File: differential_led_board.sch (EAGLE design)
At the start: 51 parts, among them IC1 LD1117S33, IC2 TJA1057, IC3 AT25SF041, IC4 LMS33460, IC5 SN75175SOP-16, IC6 STM32F042F, J1 1792863, Q1 8MHz

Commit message: Finished output stage of differential LED board; started routing CANnabus controller/power sections
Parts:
- added R11, R12: 1k, rcl:R-EU_M0805
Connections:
- removed net ADC_VCC: IC6.PA0
- new net ADC_VIN: IC6.PA0, R11.1, R12.2
- net +5V: now also R11.2
- net GND: now also R12.1
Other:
- note added: "VIn Measurement"
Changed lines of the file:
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@@
 <attribute name="MOUSER" value="71-CRCW0805330RFKEAC"/>
 </part>
+<part name="R11" library="rcl" library_urn="urn:adsk.eagle:library:334" deviceset="R-EU_" device="M0805" package3d_urn="urn:adsk.eagle:package:23556/1" value="1k">
+<attribute name="MOUSER" value="755-ESR10EZPJ102"/>
+</part>
+<part name="R12" library="rcl" library_urn="urn:adsk.eagle:library:334" deviceset="R-EU_" device="M0805" package3d_urn="urn:adsk.eagle:package:23556/1" value="1k">
+<attribute name="MOUSER" value="755-ESR10EZPJ102"/>
+</part>
+<part name="GND19" library="supply1" library_urn="urn:adsk.eagle:library:371" deviceset="GND" device=""/>
+<part name="P+14" library="supply1" library_urn="urn:adsk.eagle:library:371" deviceset="+5V" device=""/>
 </parts>
 <sheets>
@@
 <text x="149.86" y="38.1" size="2.54" layer="97">CAN Transceiver</text>
 <text x="101.6" y="149.86" size="2.54" layer="97">Boot Flash</text>
+<wire x1="147.32" y1="83.82" x2="147.32" y2="147.32" width="0.1524" layer="94" style="longdash"/>
+<text x="101.6" y="86.36" size="2.54" layer="97">VIn Measurement</text>
 </plain>
 <instances>
@@
 <instance part="GND11" gate="1" x="55.88" y="7.62" smashed="yes">
 <attribute name="VALUE" x="53.34" y="5.08" size="1.778" layer="96"/>
+</instance>
+<instance part="R11" gate="G$1" x="106.68" y="134.62" smashed="yes" rot="R90">
+<attribute name="MOUSER" x="106.68" y="134.62" size="1.27" layer="96" rot="R90" align="top-center" display="off"/>
+<attribute name="NAME" x="105.1814" y="130.81" size="1.778" layer="95" rot="R90"/>
+<attribute name="VALUE" x="109.982" y="133.35" size="1.778" layer="96" rot="R90"/>
+</instance>
+<instance part="R12" gate="G$1" x="106.68" y="124.46" smashed="yes" rot="R90">
+<attribute name="MOUSER" x="106.68" y="124.46" size="1.27" layer="96" rot="R90" align="top-center" display="off"/>
+<attribute name="NAME" x="105.1814" y="120.65" size="1.778" layer="95" rot="R90"/>
+<attribute name="VALUE" x="109.982" y="123.19" size="1.778" layer="96" rot="R90"/>
+</instance>
+<instance part="GND19" gate="1" x="106.68" y="116.84" smashed="yes">
+<attribute name="VALUE" x="104.14" y="114.3" size="1.778" layer="96"/>
+</instance>
+<instance part="P+14" gate="1" x="106.68" y="142.24" smashed="yes">
+<attribute name="VALUE" x="104.14" y="137.16" size="1.778" layer="96" rot="R90"/>
 </instance>
 </instances>
@@
 <junction x="198.12" y="53.34"/>
 </segment>
+<segment>
+<pinref part="R12" gate="G$1" pin="1"/>
+<pinref part="GND19" gate="1" pin="GND"/>
+<junction x="106.68" y="119.38"/>
+</segment>
 </net>
 <net name="CAN_TX" class="0">
@@
 </segment>
 </net>
-<net name="ADC_VCC" class="0">
+<net name="ADC_VIN" class="0">
 <segment>
 <pinref part="IC6" gate="G$1" pin="PA0"/>
@@
 <junction x="68.58" y="149.86"/>
 </segment>
+<segment>
+<pinref part="R11" gate="G$1" pin="1"/>
+<pinref part="R12" gate="G$1" pin="2"/>
+<wire x1="106.68" y1="129.54" x2="111.76" y2="129.54" width="0.1524" layer="91" style="longdash"/>
+<junction x="106.68" y="129.54"/>
+<label x="111.76" y="129.54" size="1.27" layer="95" xref="yes"/>
+</segment>
 </net>
 <net name="ADC_CURRENT" class="0">
@@
 <junction x="66.04" y="17.78"/>
 </segment>
-</net>
+<segment>
+<pinref part="R11" gate="G$1" pin="2"/>
+<pinref part="P+14" gate="1" pin="+5V"/>
+<junction x="106.68" y="139.7"/>
+</segment>
+</net>

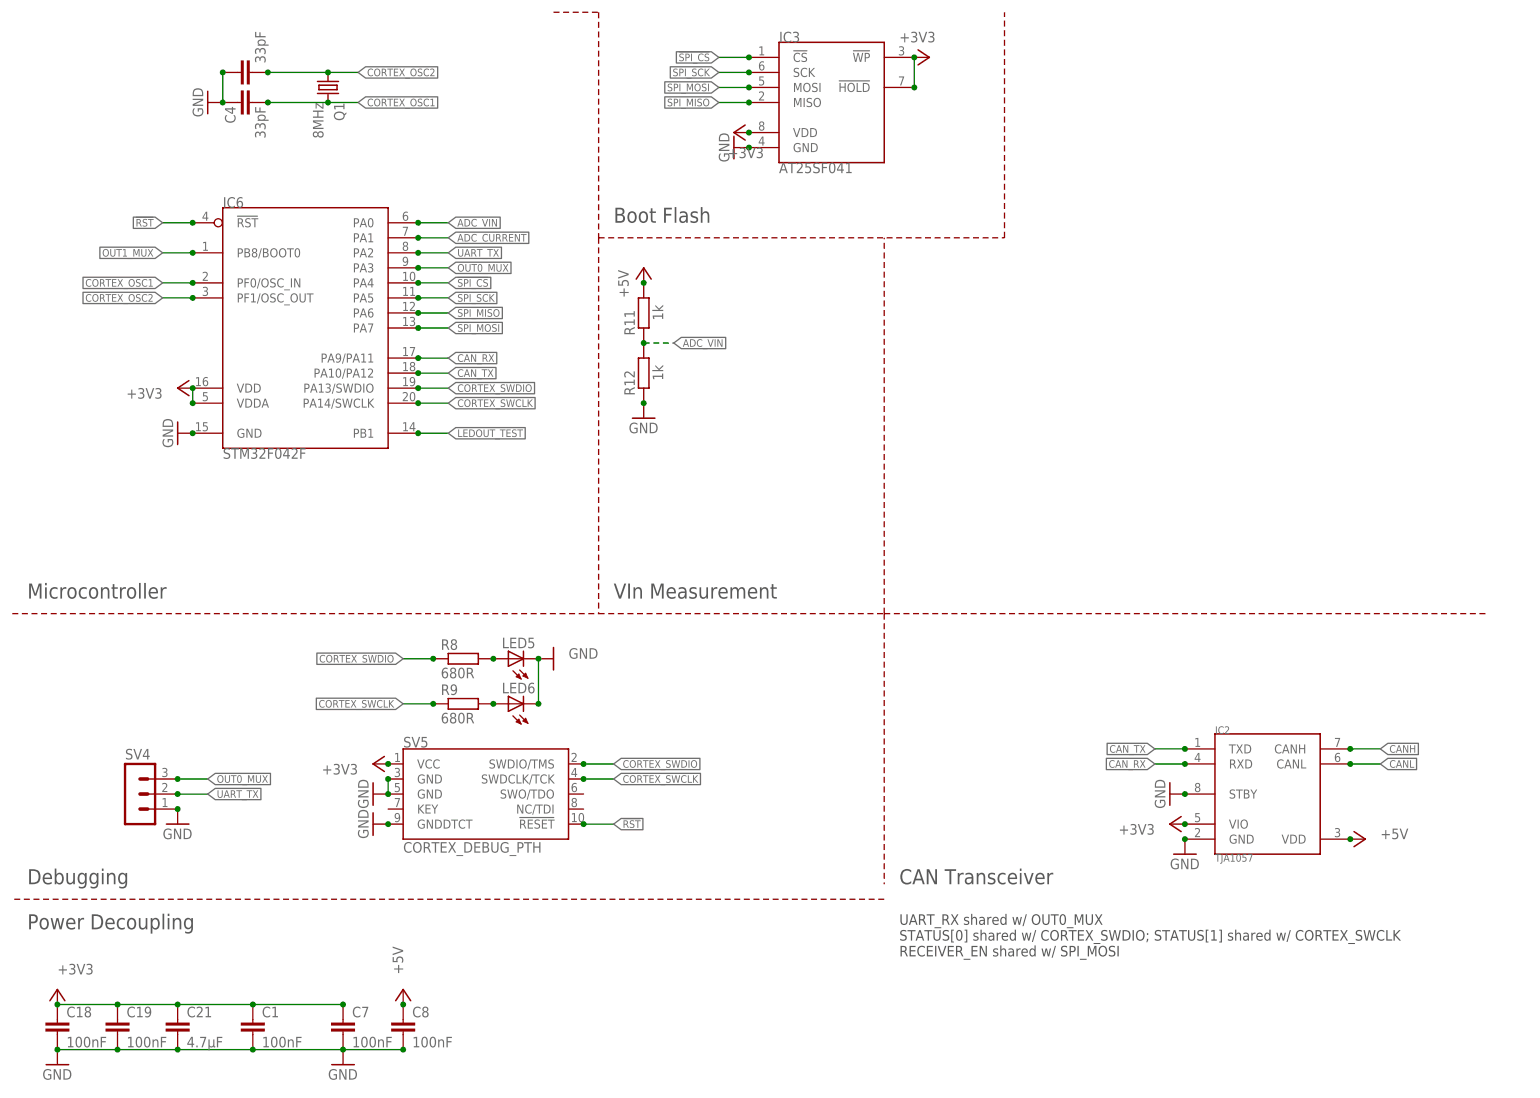
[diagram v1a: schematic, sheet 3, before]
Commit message: Added LT6100 to measure current (todo: add shunt connections)
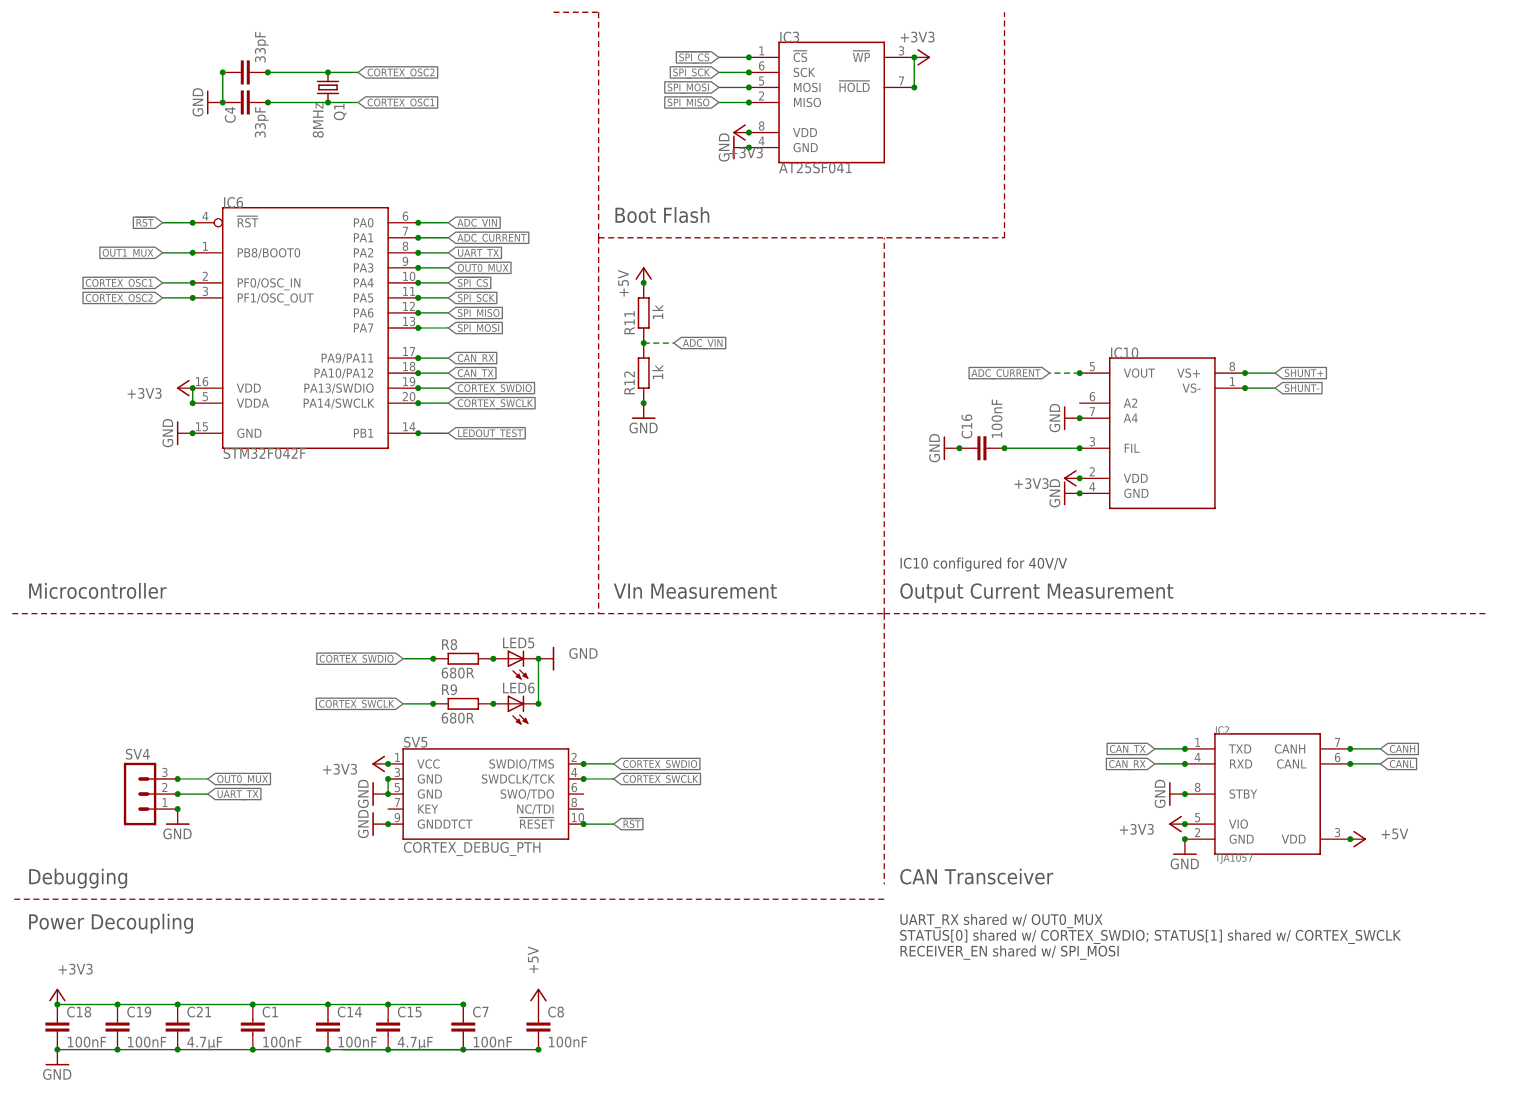
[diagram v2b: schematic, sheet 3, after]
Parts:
- added C14, C16: 100nF, rcl:C-EUC0805
- added C15: 4.7µF, rcl:C-EUC0805
- added IC10: (no value), lichtenstein_onion:LT6100MSOP-8
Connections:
- new net N$7: C16.2, IC10.FIL
- new net SHUNT+: IC10.VS+
- new net SHUNT-: IC10.VS-
- net +3V3: now also C14.1, C15.1, IC10.VDD
- net ADC_CURRENT: now also IC10.VOUT
- net GND: now also C14.2, C15.2, C16.1, IC10.A4, IC10.GND
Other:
- note added: "IC10 configured for 40V/V"
- note added: "Output Current Measurement"
- moved on the sheet: C7, C8

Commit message: finished routing LED board; substituted a few components and fixed missing level translation
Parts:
- removed C21: 4.7µF, rcl:C-EUC0805
- removed LED5: (no value), led:LEDCHIPLED_1206
- added C17: 4.7µF, rcl:C-EUC0805
- added C20: 100nF, rcl:C-EUC0805
- added LED2: GRN, led:LEDCHIPLED_1206
- added R13: 1k, rcl:R-EU_M0805
- C11: value 470µF -> 100nF; device rcl:CPOL-EUUD-8X10 -> rcl:C-EUC0805; MOUSER 647-UWT1C471MNL1S -> 710-885012207072
- C12: value 100nF -> 4.7µF; MOUSER 710-885012207072 -> 81-GRM21BR71A475ME1L
- C13, C14: value 100nF -> 33pF; MOUSER 710-885012207072 -> 710-885012007013
- C15: value 4.7µF -> 100nF; MOUSER 81-GRM21BR71A475ME1L -> 710-885012207072
- C16: MOUSER 710-885012007059 -> 710-885012207072
- C2: value 33pF -> 100nF; MOUSER 710-885012007013 -> 710-885012207072
- C3: value 100nF -> 470µF; device rcl:C-EUC0805 -> rcl:CPOL-EUUD-8X10; MOUSER 710-885012207072 -> 647-UWT1C471MNL1S
- C4: value 33pF -> 47µF; device rcl:C-EUC0805 -> rcl:CPOL-EUCT6032; MOUSER 710-885012007013 -> 581-TAJD476M016RNJV
- C6: value 47µF -> 100nF; device rcl:CPOL-EUCT6032 -> rcl:C-EUC0805; MOUSER 581-TAJD476M016RNJV -> 710-885012207072
- IC1: value LD1117S33 -> SN75175SOP-16; device lichtenstein_onion:LM1117SOT223 -> lichtenstein_onion:SN75175SOP-16
- IC10: value (none) -> TJA1057; device lichtenstein_onion:LT6100MSOP-8 -> lichtenstein_onion:TJA1057
- IC2: value TJA1057 -> (none); device lichtenstein_onion:TJA1057 -> lichtenstein_onion:TLV803SOT-23
- IC3: value AT25SF041 -> LD1117S33; device lichtenstein_onion:AT25SF041 -> lichtenstein_onion:LM1117SOT223
- IC4: value LMS33460 -> 74LVC1G157; device lichtenstein_onion:LMS33460SC70-5 -> lichtenstein_onion:74LVC1G157SOT457
- IC5: value SN75175SOP-16 -> 74LVC1G157; device lichtenstein_onion:SN75175SOP-16 -> lichtenstein_onion:74LVC1G157SOT457
- IC6: value STM32F042F -> CD40109B; device lichtenstein_onion:STM32F042F -> lichtenstein_onion:CD40109BSO-16
- IC7: value (none) -> STM32F042F; device lichtenstein_onion:74LVC1T45SOT26 -> lichtenstein_onion:STM32F042F
- IC8: value (none) -> AT25SF041; device lichtenstein_onion:74LVC1G157SOT457 -> lichtenstein_onion:AT25SF041
- IC9: value (none) -> LT6100; device lichtenstein_onion:74LVC1G157SOT457 -> lichtenstein_onion:LT6100MSOP-8
- J1: value 1792863 -> CORTEX_DEBUG_PTH; device lichtenstein_onion:1792863 -> lichtenstein_onion:CORTEX_DEBUG_PTH
- LED1, LED3, LED4: value (none) -> GRN
- R10: value 330R -> 680R; MOUSER 71-CRCW0805330RFKEAC -> 652-CR0805-FX6800GLF
- R11: value 1k -> 680R; MOUSER 755-ESR10EZPJ102 -> 652-CR0805-FX6800GLF
- R2: value 680R -> 100R; device rcl:R-EU_M0805 -> rcl:R-EU_M1206; MOUSER 652-CR0805-FX6800GLF -> 652-CR1206FX-1000ELF
- R3: value 1k -> 10k; MOUSER 755-ESR10EZPJ102 -> 755-ESR10EZPJ103
- R4: value 100R -> 680R; device rcl:R-EU_M1206 -> rcl:R-EU_M0805; MOUSER 652-CR1206FX-1000ELF -> 652-CR0805-FX6800GLF
- R5: value 10k -> 1k; MOUSER 755-ESR10EZPJ103 -> 755-ESR10EZPJ102
- R7: value 330R -> 10k; MOUSER 71-CRCW0805330RFKEAC -> 755-ESR10EZPJ103
- R8, R9: value 680R -> 330R; MOUSER 652-CR0805-FX6800GLF -> 71-CRCW0805330RFKEAC
- SV2: value 1792889 -> 1792863; device lichtenstein_onion:1792889 -> lichtenstein_onion:1792863
- SV4: value (none) -> 1792889; device con-lstb:MA03-1 -> lichtenstein_onion:1792889
- SV5: value CORTEX_DEBUG_PTH -> (none); device lichtenstein_onion:CORTEX_DEBUG_PTH -> con-lstb:MA03-1
- renumbered LED6 to LED4
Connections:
- new net OUT0_MUX_5V: IC4.SEL, IC6.E
- new net OUT1_MUX_5V: IC5.SEL, IC6.G
- net !RST: now also IC2.!RESET, IC7.!RST, J1.!RESET, R3.1; no longer IC4.VOUT, IC6.!RST, SV5.!RESET
- net !SPI_CS: now also IC7.PA4, IC8.!CS; no longer IC3.!CS, IC6.PA4
- net +3V3: now also C10.1, C11.1, C12.1, C16.1, C17.1, C2.1, C4.+, C5.1, C9.1, IC10.VIO, IC2.VDD, IC3.OUT, IC6.EN_A, IC6.EN_B, IC6.EN_C, IC6.VCCA, IC7.VDD, IC8.!HOLD, IC8.!WP, IC8.VDD, IC9.VDD, J1.VCC, R3.2, R4.1; no longer C1.1, C13.1, C14.1, C19.1, C21.1, C3.1, C6.+, C7.1, IC1.OUT, IC10.VDD, IC2.VIO, IC3.!HOLD, IC3.!WP, IC3.VDD, IC4.VIN, IC6.VDD, IC6.VDDA, IC7.DIR, R2.1, SV5.VCC
- net +5V: now also C1.1, C19.1, C3.+, C6.1, C7.1, IC1.VCC, IC10.VDD, IC3.IN, IC4.VDD, IC5.VDD, IC6.VCCB, R12.2, R5.1, SV2.2, SV4.4; no longer C10.1, C11.+, C12.1, C5.1, C9.1, IC1.IN, IC2.VDD, IC5.VCC, IC7.VDDB, IC8.VDD, IC9.VDD, J1.2, R11.2, R3.1, SV2.4
- net ADC_CURRENT: now also IC7.PA1, IC9.VOUT; no longer IC10.VOUT, IC6.PA1
- net ADC_VIN: now also IC7.PA0, R12.1, R13.2; no longer IC6.PA0, R11.1, R12.2
- net CANH: now also IC10.CANH; no longer IC2.CANH
- net CANL: now also IC10.CANL; no longer IC2.CANL
- net CAN_RX: now also IC10.RXD, IC7.PA9/PA11; no longer IC2.RXD, IC6.PA9/PA11
- net CAN_TX: now also IC10.TXD, IC7.PA10/PA12; no longer IC2.TXD, IC6.PA10/PA12
- net CORTEX_OSC1: now also C14.2, IC7.PF0/OSC_IN; no longer C4.2, IC6.PF0/OSC_IN
- net CORTEX_OSC2: now also C13.2, IC7.PF1/OSC_OUT; no longer C2.2, IC6.PF1/OSC_OUT
- net CORTEX_SWCLK: now also IC7.PA14/SWCLK, J1.SWDCLK/TCK, R11.1; no longer IC6.PA14/SWCLK, R9.1, SV5.SWDCLK/TCK
- net CORTEX_SWDIO: now also IC7.PA13/SWDIO, J1.SWDIO/TMS, R10.1; no longer IC6.PA13/SWDIO, R8.1, SV5.SWDIO/TMS
- net GND: now also C11.2, C13.1, C14.1, C16.2, C17.2, C2.2, C20.1, C3.-, C4.-, C6.2, IC1.EN34, IC10.STBY, IC6.EN_D, IC9.A4, J1.GND@3, J1.GND@5, J1.GNDDTCT, LED2.C, R13.1, R7.1, SV2.1, SV4.2, SV4.3, SV5.1; no longer C11.-, C13.2, C14.2, C16.1, C2.1, C21.2, C3.2, C4.1, C6.-, IC10.A4, IC2.STBY, IC5.EN34, J1.1, LED5.C, R12.1, R5.1, SV2.2, SV2.3, SV4.1, SV5.GND@3, SV5.GND@5, SV5.GNDDTCT
- net LEDOUT0: now also IC1.1Y, IC4.I0; no longer IC5.1Y, IC8.I0
- net LEDOUT1: now also IC1.2Y, IC5.I0; no longer IC5.2Y, IC9.I0
- net LEDOUT_TEST: now also IC6.B, IC7.PB1; no longer IC6.PB1, IC7.A
- net LEDOUT_TEST_5V: now also IC4.I1, IC5.I1, IC6.F; no longer IC7.B, IC8.I1, IC9.I1
- net N$1: now also R4.2; no longer R2.2
- net N$2: now also LED2.A, R5.2; no longer LED3.A, R3.2
- net N$3: now also R8.1, SV4.1; no longer R10.1, SV3.1
- net N$4: now also LED3.A, R10.2; no longer LED5.A, R8.2
- net N$5: now also R11.2; no longer R9.2
- net N$6: now also R9.1, SV3.1; no longer R7.1, SV2.1
- net N$7: now also C20.2, IC9.FIL; no longer C16.2, IC10.FIL
- net OUT0: now also IC4.Y, R9.2; no longer IC8.Y, R7.2
- net OUT0_MUX: now also IC6.A, IC7.PA3, SV5.3; no longer IC6.PA3, IC8.SEL, SV4.3
- net OUT0_N: now also IC1.1B; no longer IC5.1B
- net OUT0_P: now also IC1.1A; no longer IC5.1A
- net OUT1: now also IC5.Y, R8.2; no longer IC9.Y, R10.2
- net OUT1_MUX: now also IC6.C, IC7.PB8/BOOT0, R7.2; no longer IC6.PB8/BOOT0, IC9.SEL, R5.2
- net OUT1_N: now also IC1.2B, R2.1; no longer IC5.2B, R4.1
- net OUT1_P: now also IC1.2A, R2.2; no longer IC5.2A, R4.2
- net SHUNT+: now also IC9.VS+; no longer IC10.VS+
- net SHUNT-: now also IC9.VS-; no longer IC10.VS-
- net SPI_MISO: now also IC7.PA6, IC8.MISO; no longer IC3.MISO, IC6.PA6
- net SPI_MOSI: now also IC1.EN12, IC7.PA7, IC8.MOSI; no longer IC3.MOSI, IC5.EN12, IC6.PA7
- net SPI_SCK: now also IC7.PA5, IC8.SCK; no longer IC3.SCK, IC6.PA5
- net UART_TX: now also IC7.PA2, SV5.2; no longer IC6.PA2, SV4.2
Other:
- note added: "Test Output/MUX Control Level Conversion"
- note removed: "Test Output Level Conversion"
